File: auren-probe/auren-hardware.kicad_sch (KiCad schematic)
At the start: 6 parts, among them J3 Speaker_1, J4 Speaker_2

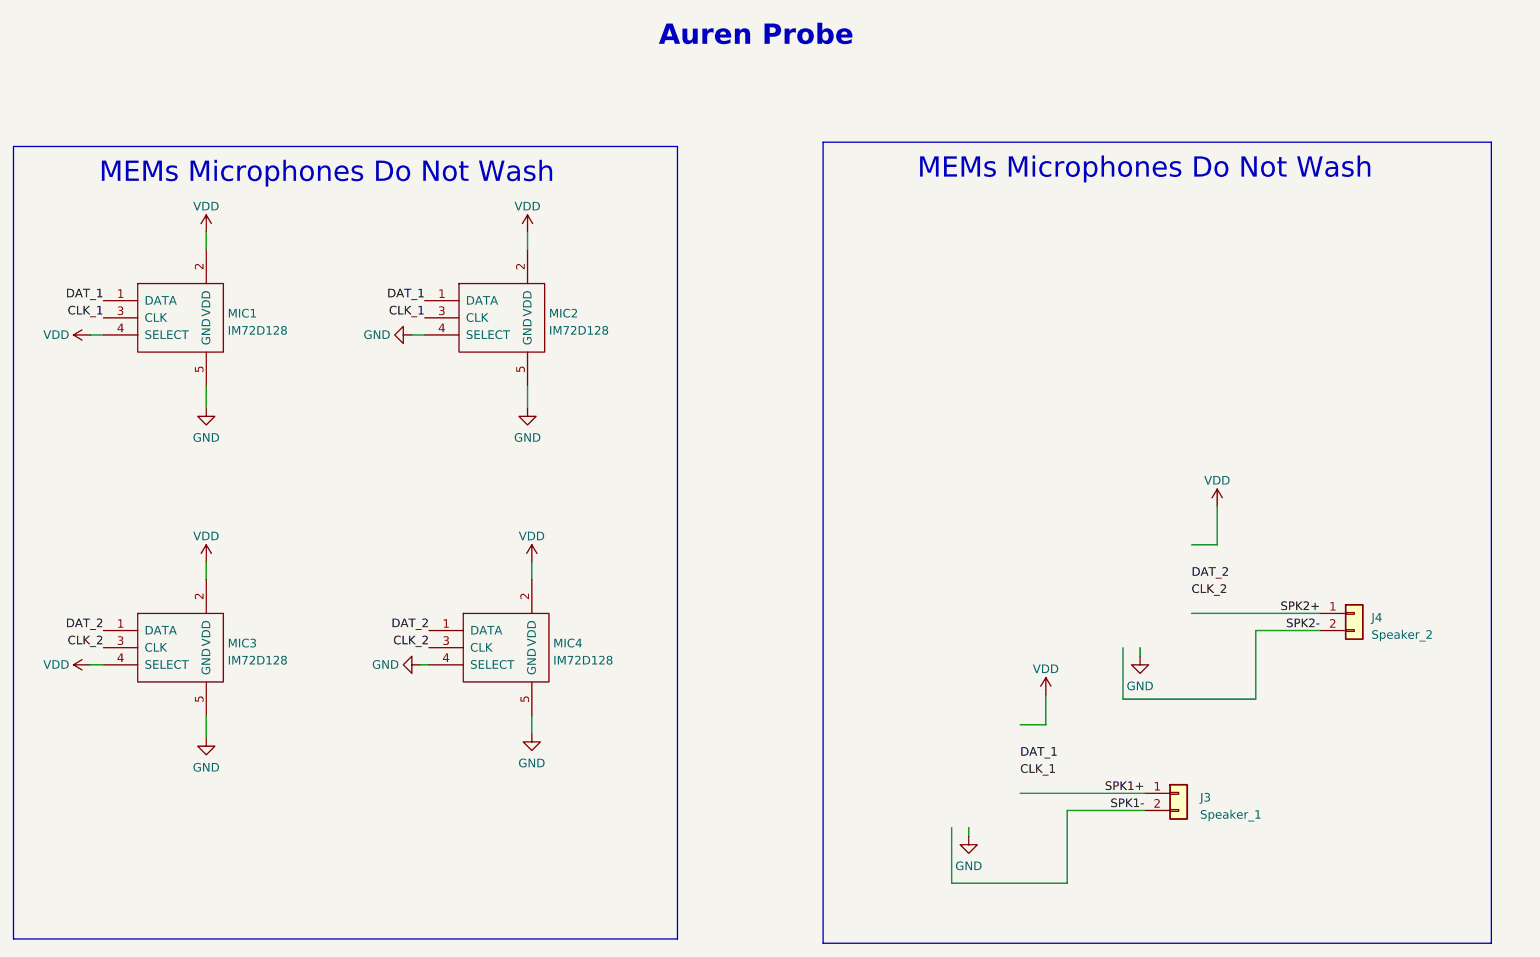
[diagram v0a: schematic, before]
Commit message: PCB Routing
Fit components and route PCB.
DRC shows mic gnd not connected. needs debugging.
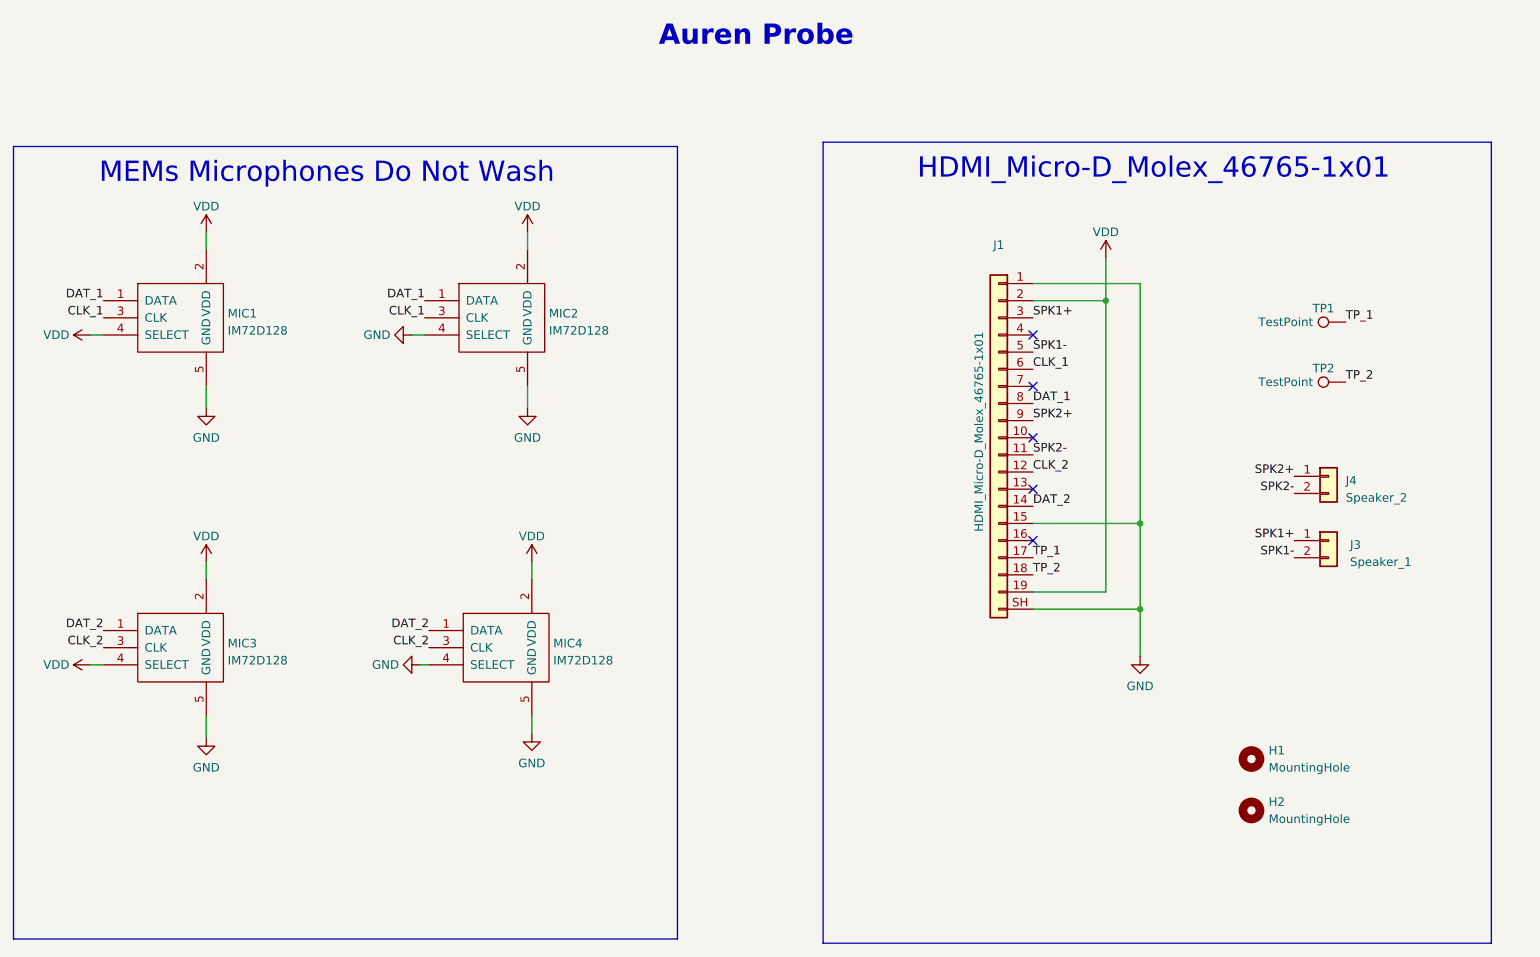
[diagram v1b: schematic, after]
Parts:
- added H1, H2: MountingHole, auren-library:MountingHole_0-80_Screw, symbol Mechanical:MountingHole
- added J1: HDMI_Micro-D_Molex_46765-1x01, Connector_Video:HDMI_Micro-D_Molex_46765-1x01, symbol Flywheel_Library:Auren_Connector_hdmi
- added TP1, TP2: TestPoint, TestPoint:TestPoint_Pad_1.0x1.0mm, symbol Connector:TestPoint
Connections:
- net CLK_1: now also J1.6 (Pin_6)
- net CLK_2: now also J1.12 (Pin_12)
- net DAT_1: now also J1.8 (Pin_8)
- net DAT_2: now also J1.14 (Pin_14)
- net GND: now also J1.1 (Pin_1), J1.15 (Pin_15), J1.SH (Pin_20)
- net SPK1+: now also J1.3 (Pin_3)
- net SPK1-: now also J1.5 (Pin_5)
- net SPK2+: now also J1.9 (Pin_9)
- net SPK2-: now also J1.11 (Pin_11)
- net VDD: now also J1.19 (Pin_19), J1.2 (Pin_2)
- new net TP_1: J1.17 (Pin_17), TP1.1
- new net TP_2: J1.18 (Pin_18), TP2.1
- no-connect marks 0 -> 5
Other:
- note added: "HDMI_Micro-D_Molex_46765-1x01"
- moved on the sheet: J3, J4
